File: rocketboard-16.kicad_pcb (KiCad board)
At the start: 2 copper layers, 86.2 x 99.9 mm, 110 parts, among them J1 SWD, K1 MX_RGB, K10 MX_RGB, K11 MX_RGB, K12 MX_RGB, K13 MX_RGB, K14 MX_RGB, K15 MX_RGB, K16 MX_RGB, K2 MX_RGB, K3 MX_RGB, K4 MX_RGB, K5 MX_RGB, K6 MX_RGB, K7 MX_RGB, K8 MX_RGB, K9 MX_RGB, P1 USB_C_Plug_USB2.0, SW1 SW_Push, SW2 Rotary 1, SW3 Rotary 2, U1 STM32F103C8T6, U2 AMS1117-3.3, U3 USBLC6-2SC6, U4 SSD1306_128x64, X1 8 MHz, Y1 32.768 kHz

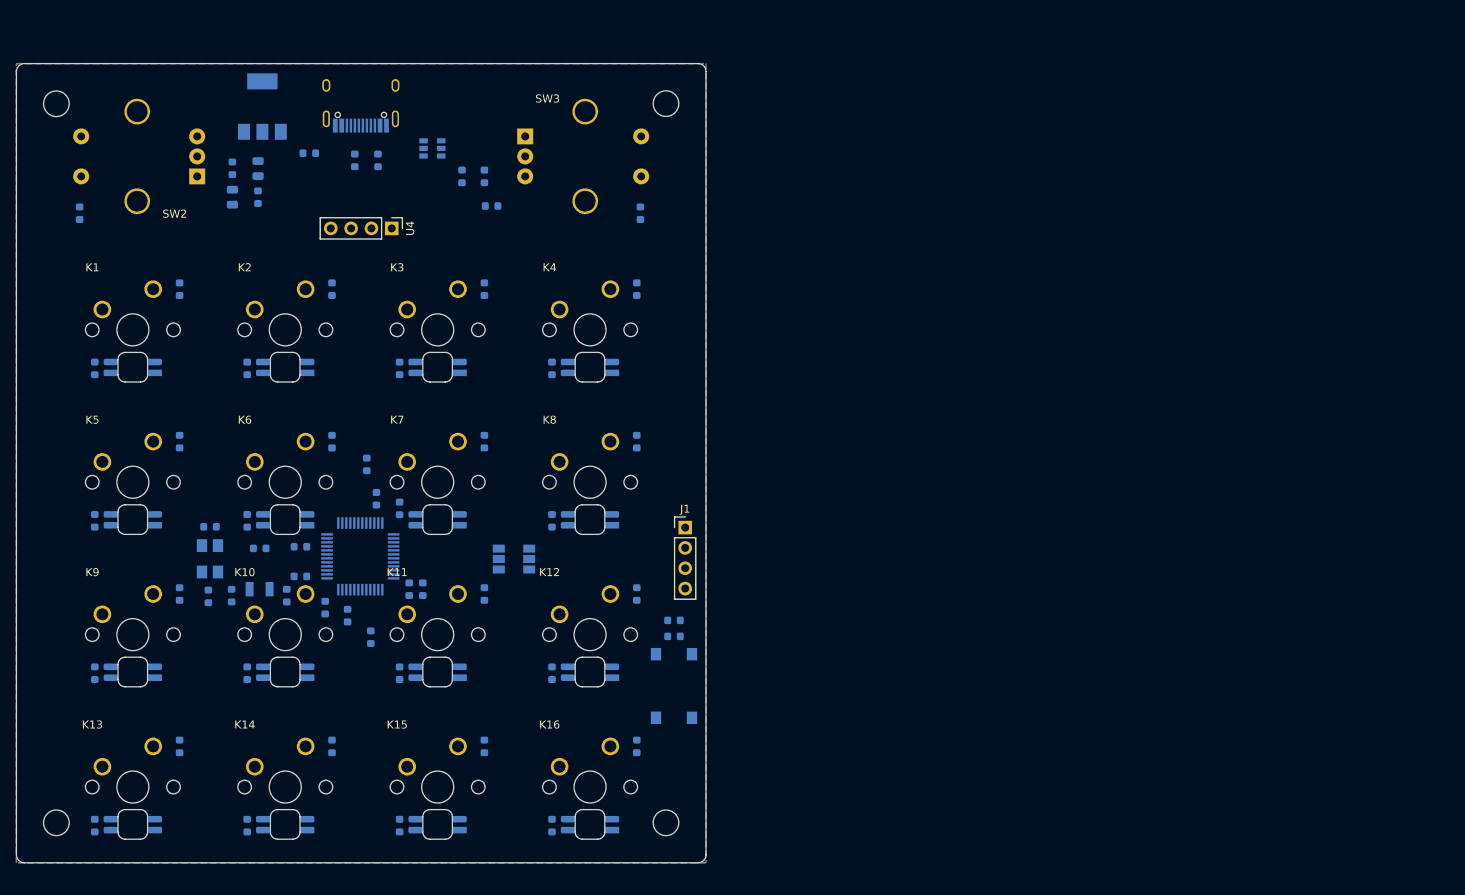
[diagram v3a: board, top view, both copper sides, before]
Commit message: Extended PCB height to accomodate the OLED display. Changed the board color to black for previews. Moved components up to take up new space from increasing height of board.
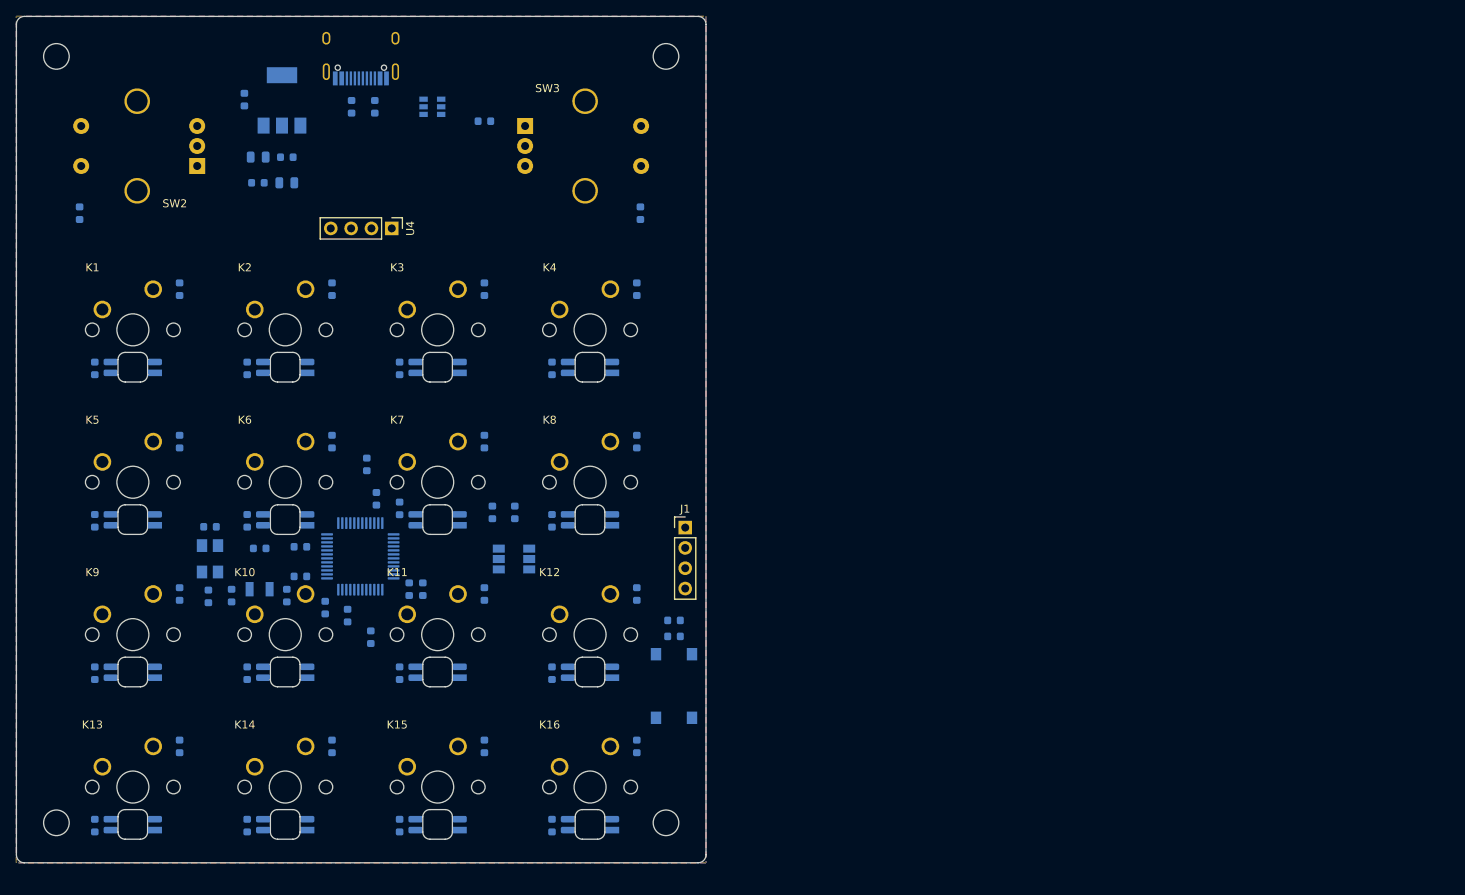
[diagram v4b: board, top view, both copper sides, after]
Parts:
- moved R1 42.5 mm to (142.3, 107.5), turned to 270 degrees
- moved R2 42.0 mm to (139.5, 107.5), turned to 270 degrees
- moved R6 10.6 mm to (138.5, 58.6)
- moved D17 10.5 mm to (108.5, 55.9), turned to 90 degrees
- moved C13 7.03 mm to (113.8, 66.3), turned to 180 degrees
- moved R5 6.71 mm to (124.8, 56.8)
- moved R4 6.71 mm to (121.9, 56.8)
- moved C14 6.16 mm to (113.8, 63.1), turned to 180 degrees
- moved H1 5.92 mm to (85.0, 50.5)
- moved H2 5.90 mm to (161.2, 50.5)
- moved P1 5.90 mm to (123.1, 50.1)
- moved U3 5.20 mm to (132.0, 56.8)
- moved C4 3.67 mm to (110.2, 66.3), turned to 0 degrees
- moved U2 2.57 mm to (113.2, 56.0)
- moved G*** 1.92 mm to (85.3, 124.8)
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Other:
- board size 86.2 x 99.9 mm -> 86.2 x 105.8 mm

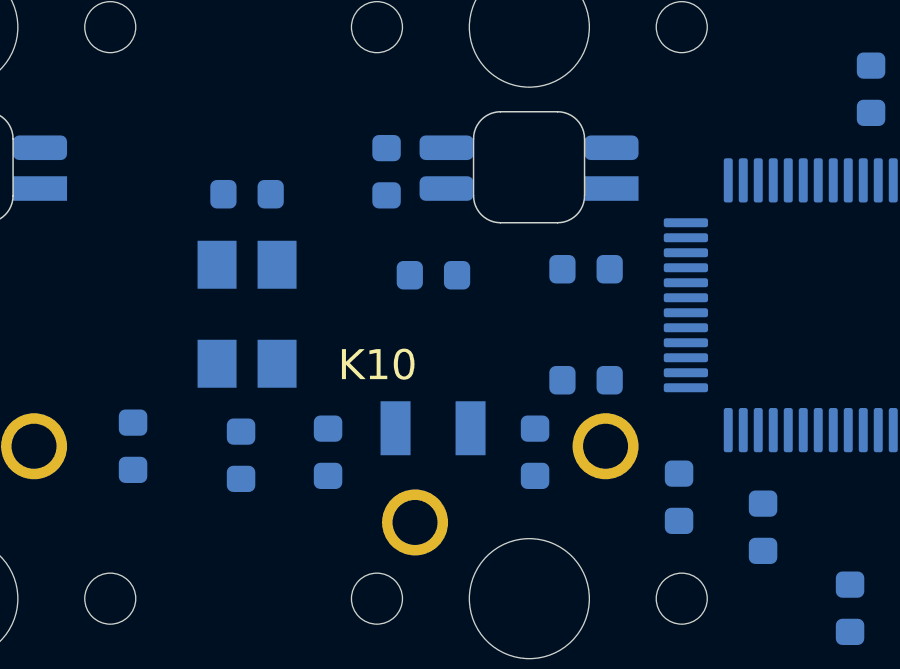
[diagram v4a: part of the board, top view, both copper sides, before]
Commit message: Routed the two crystals
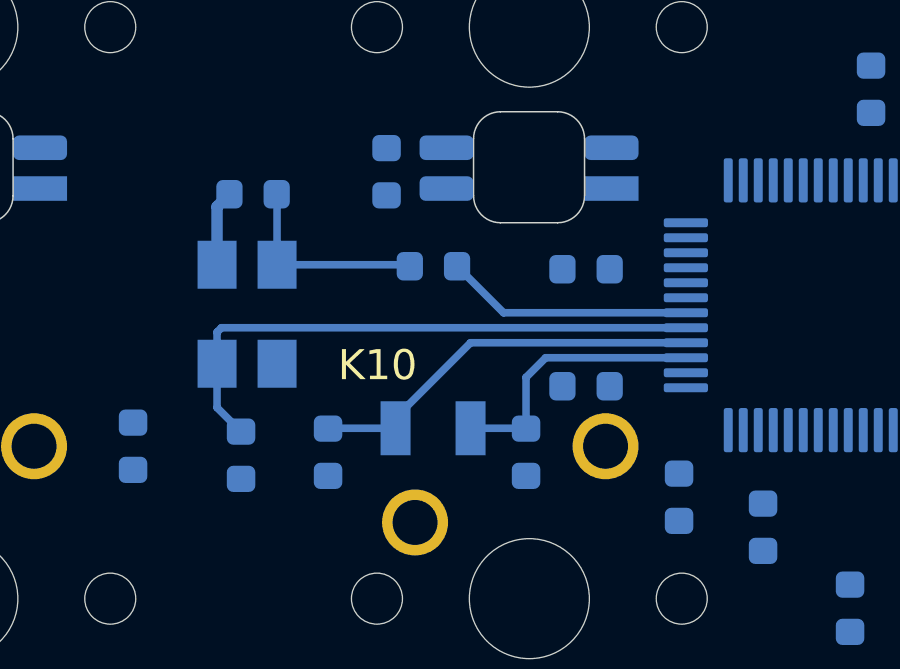
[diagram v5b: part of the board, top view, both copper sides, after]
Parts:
- moved C3 0.30 mm to (113.5, 117.9)
- moved R7 0.30 mm to (110.4, 111.7)
- moved C2 0.20 mm to (104.4, 109.3)
- moved C6 0.20 mm to (115.5, 115.7)
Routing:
- net OSC_IN: track 0.00 -> 19.3 mm
- net OSC32_OUT: track 0.00 -> 13.3 mm
- net OSC32_IN: track 0.00 -> 9.18 mm
- net OSC_OUT: track 0.00 -> 8.27 mm
- net Net-(C2-Pad1): track 0.00 -> 6.80 mm
- net GND: track 0.00 -> 2.52 mm
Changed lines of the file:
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@@
     (thickness 1.6)
     (drawings 13)
-    (tracks 0)
+    (tracks 24)
     (zones 0)
     (modules 110)
@@
   )
   (module Capacitor_SMD:C_0603_1608Metric (layer B.Cu)
-    (at 115.5 115.5)
+    (at 115.5 115.7)
     (descr "Capacitor SMD 0603 (1608 Metric), square (rectangular) end terminal, IPC_7351 nominal, (Body size source: http://www.tortai-tech.com/upload/download/2011102023233369053.pdf), generated with kicad-footprint-generator")
     (tags capacitor)
@@
   )
   (module Capacitor_SMD:C_0603_1608Metric (layer B.Cu)
-    (at 113.8 117.9 270)
+    (at 113.5 117.9 270)
     (descr "Capacitor SMD 0603 (1608 Metric), square (rectangular) end terminal, IPC_7351 nominal, (Body size source: http://www.tortai-tech.com/upload/download/2011102023233369053.pdf), generated with kicad-footprint-generator")
     (tags capacitor)
@@
       (effects (font (size 1 1) (thickness 0.15)) (justify mirror))
     )
-    (fp_line (start 1.48 -0.73) (end -1.48 -0.73) (layer B.CrtYd) (width 0.05))
-    (fp_line (start 1.48 0.73) (end 1.48 -0.73) (layer B.CrtYd) (width 0.05))
-    (fp_line (start -1.48 0.73) (end 1.48 0.73) (layer B.CrtYd) (width 0.05))
-    (fp_line (start -1.48 -0.73) (end -1.48 0.73) (layer B.CrtYd) (width 0.05))
-    (fp_line (start -0.162779 -0.51) (end 0.162779 -0.51) (layer B.SilkS) (width 0.12))
-    (fp_line (start -0.162779 0.51) (end 0.162779 0.51) (layer B.SilkS) (width 0.12))
-    (fp_line (start 0.8 -0.4) (end -0.8 -0.4) (layer B.Fab) (width 0.1))
-    (fp_line (start 0.8 0.4) (end 0.8 -0.4) (layer B.Fab) (width 0.1))
-    (fp_line (start -0.8 0.4) (end 0.8 0.4) (layer B.Fab) (width 0.1))
-    (fp_line (start -0.8 -0.4) (end -0.8 0.4) (layer B.Fab) (width 0.1))
     (fp_text user %R (at 0 0 270) (layer B.Fab)
       (effects (font (size 0.4 0.4) (thickness 0.06)) (justify mirror))
     )
-    (pad 2 smd roundrect (at 0.7875 0 270) (size 0.875 0.95) (layers B.Cu B.Paste B.Mask) (roundrect_rratio 0.25)
-      (net 24 GND))
+    (fp_line (start -0.8 -0.4) (end -0.8 0.4) (layer B.Fab) (width 0.1))
+    (fp_line (start -0.8 0.4) (end 0.8 0.4) (layer B.Fab) (width 0.1))
+    (fp_line (start 0.8 0.4) (end 0.8 -0.4) (layer B.Fab) (width 0.1))
+    (fp_line (start 0.8 -0.4) (end -0.8 -0.4) (layer B.Fab) (width 0.1))
+    (fp_line (start -0.162779 0.51) (end 0.162779 0.51) (layer B.SilkS) (width 0.12))
+    (fp_line (start -0.162779 -0.51) (end 0.162779 -0.51) (layer B.SilkS) (width 0.12))
+    (fp_line (start -1.48 -0.73) (end -1.48 0.73) (layer B.CrtYd) (width 0.05))
+    (fp_line (start -1.48 0.73) (end 1.48 0.73) (layer B.CrtYd) (width 0.05))
+    (fp_line (start 1.48 0.73) (end 1.48 -0.73) (layer B.CrtYd) (width 0.05))
+    (fp_line (start 1.48 -0.73) (end -1.48 -0.73) (layer B.CrtYd) (width 0.05))
     (pad 1 smd roundrect (at -0.7875 0 270) (size 0.875 0.95) (layers B.Cu B.Paste B.Mask) (roundrect_rratio 0.25)
       (net 27 OSC32_IN))
+    (pad 2 smd roundrect (at 0.7875 0 270) (size 0.875 0.95) (layers B.Cu B.Paste B.Mask) (roundrect_rratio 0.25)
+      (net 24 GND))
     (model ${KISYS3DMOD}/Capacitor_SMD.3dshapes/C_0603_1608Metric.wrl
       (at (xyz 0 0 0))
@@
   )
   (module Resistor_SMD:R_0603_1608Metric (layer B.Cu)
-    (at 110.4125 112)
+    (at 110.4125 111.7)
     (descr "Resistor SMD 0603 (1608 Metric), square (rectangular) end terminal, IPC_7351 nominal, (Body size source: http://www.tortai-tech.com/upload/download/2011102023233369053.pdf), generated with kicad-footprint-generator")
     (tags resistor)
@@
   )
   (module Capacitor_SMD:C_0603_1608Metric (layer B.Cu)
-    (at 104.2 109.3 180)
+    (at 104.4 109.3 180)
     (descr "Capacitor SMD 0603 (1608 Metric), square (rectangular) end terminal, IPC_7351 nominal, (Body size source: http://www.tortai-tech.com/upload/download/2011102023233369053.pdf), generated with kicad-footprint-generator")
     (tags capacitor)
@@
     (arrow2b (pts (xy 80 41.4) (xy 81.126504 40.813579)))
   )
+  (segment (start 103.2 109.7125) (end 103.6125 109.3) (width 0.381) (layer B.Cu) (net 24))
+  (segment (start 103.2 111.65) (end 103.2 109.7125) (width 0.381) (layer B.Cu) (net 24))
+  (segment (start 103.2 116.4125) (end 104 117.2125) (width 0.254) (layer B.Cu) (net 25))
+  (segment (start 103.2 114.95) (end 103.2 116.4125) (width 0.254) (layer B.Cu) (net 25))
+  (segment (start 103.346 113.75) (end 118.8275 113.75) (width 0.254) (layer B.Cu) (net 25))
+  (segment (start 103.2 113.896) (end 103.346 113.75) (width 0.254) (layer B.Cu) (net 25))
+  (segment (start 103.2 114.95) (end 103.2 113.896) (width 0.254) (layer B.Cu) (net 25))
+  (segment (start 105.2 109.3125) (end 105.1875 109.3) (width 0.254) (layer B.Cu) (net 26))
+  (segment (start 105.2 111.65) (end 105.2 109.3125) (width 0.254) (layer B.Cu) (net 26))
+  (segment (start 109.575 111.65) (end 109.625 111.7) (width 0.254) (layer B.Cu) (net 26))
+  (segment (start 105.2 111.65) (end 109.575 111.65) (width 0.254) (layer B.Cu) (net 26))
+  (segment (start 113.7875 117.1) (end 113.8 117.1125) (width 0.254) (layer B.Cu) (net 27))
+  (segment (start 113.4875 117.1) (end 113.5 117.1125) (width 0.254) (layer B.Cu) (net 27))
+  (segment (start 111.65 117.1) (end 113.4875 117.1) (width 0.254) (layer B.Cu) (net 27))
+  (segment (start 113.5 117.1125) (end 113.5 115.40401) (width 0.254) (layer B.Cu) (net 27))
+  (segment (start 114.15401 114.75) (end 118.8275 114.75) (width 0.254) (layer B.Cu) (net 27))
+  (segment (start 113.5 115.40401) (end 114.15401 114.75) (width 0.254) (layer B.Cu) (net 27))
+  (segment (start 106.9125 117.1) (end 106.9 117.1125) (width 0.254) (layer B.Cu) (net 29))
+  (segment (start 109.15 117.1) (end 106.9125 117.1) (width 0.254) (layer B.Cu) (net 29))
+  (segment (start 109.15 117.1) (end 109.15 116.75) (width 0.254) (layer B.Cu) (net 29))
+  (segment (start 111.65 114.25) (end 118.8275 114.25) (width 0.254) (layer B.Cu) (net 29))
+  (segment (start 109.15 116.75) (end 111.65 114.25) (width 0.254) (layer B.Cu) (net 29))
+  (segment (start 112.75 113.25) (end 118.8275 113.25) (width 0.254) (layer B.Cu) (net 54))
+  (segment (start 111.2 111.7) (end 112.75 113.25) (width 0.254) (layer B.Cu) (net 54))
   (zone (net 24) (net_name GND) (layer F.Cu) (hatch edge 0.508)
     (connect_pads (clearance 0.508))

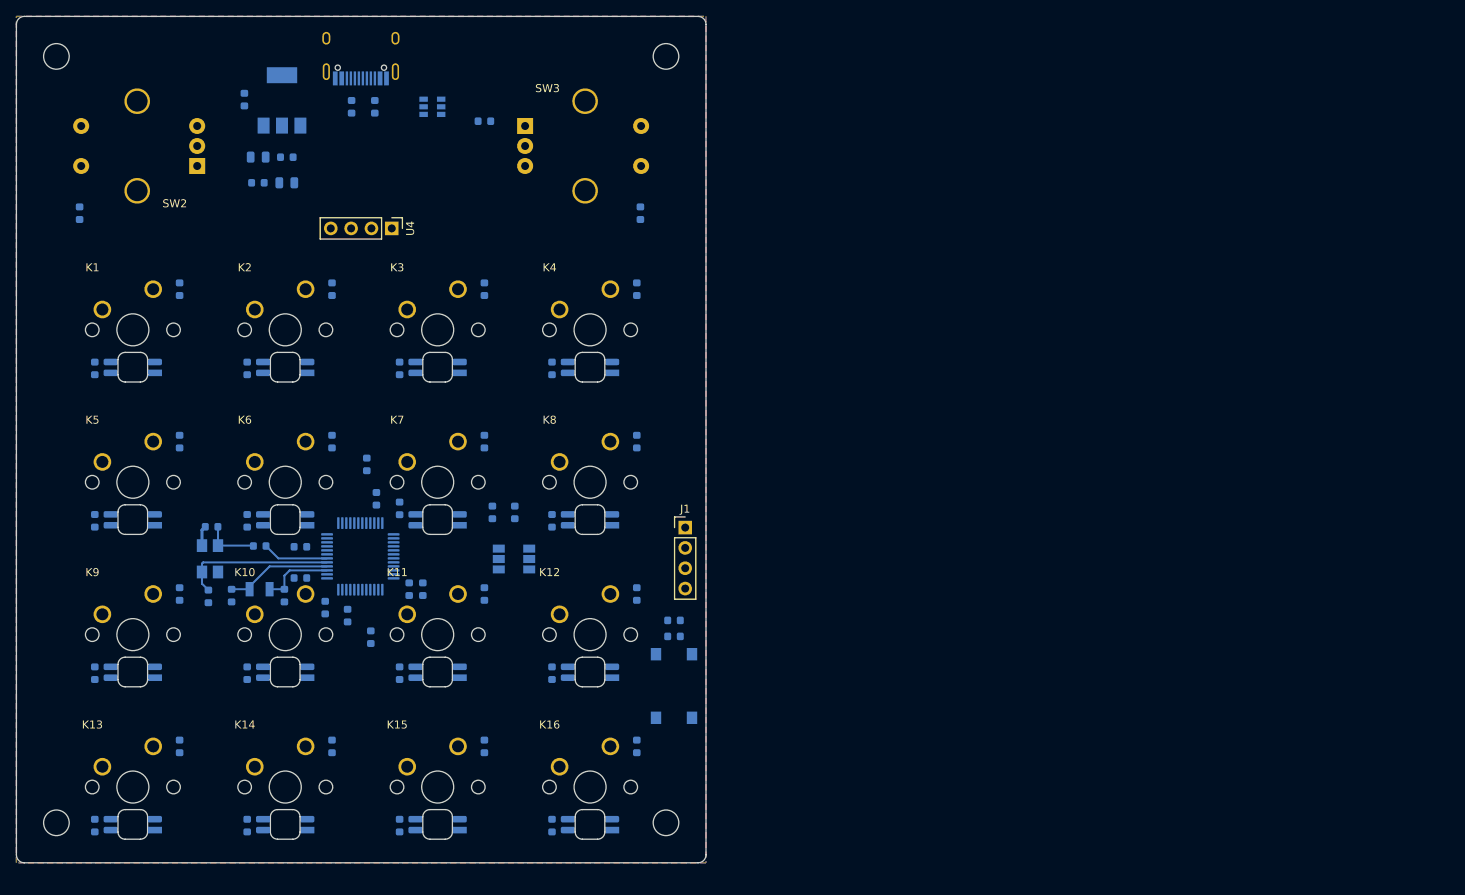
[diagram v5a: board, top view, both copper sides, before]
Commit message: Routed most of the wires, many still needed though. Changed a couple of pins around on the schematic due to simpler routing paths.
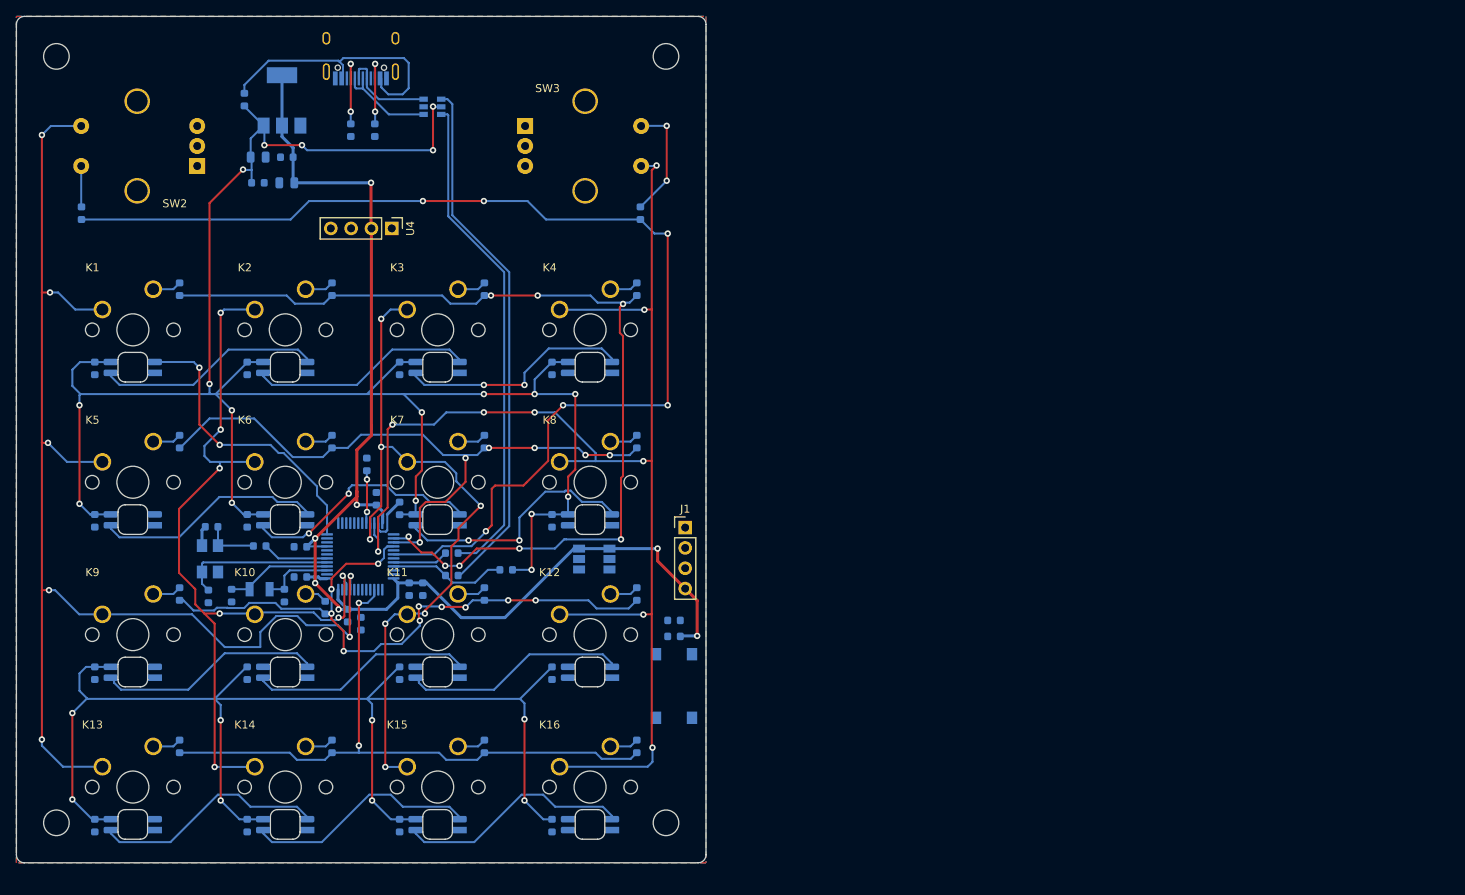
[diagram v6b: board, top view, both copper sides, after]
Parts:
- moved R6 56.1 mm to (141.2, 114.7)
- moved JP2 10.0 mm to (154.1, 113.3)
- moved JP1 10.0 mm to (150.3, 113.3)
- moved R2 9.38 mm to (134.4, 115.4), turned to 0 degrees
- moved R1 9.38 mm to (134.4, 112.6), turned to 0 degrees
- moved R4 2.92 mm to (121.8, 59.7)
- moved R5 2.92 mm to (124.8, 59.7)
- moved R8 2.09 mm to (123.1, 121.4)
- moved D18 0.24 mm to (88.1, 70.1)
- moved C6 0.13 mm to (115.5, 115.6), turned to 180 degrees
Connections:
- U1 pad 13: Row4 -> Net-(U1-Pad13)
- U1 pad 25: ROW0 -> Net-(U1-Pad25)
- U1 pad 30: Net-(U1-Pad30) -> ROW0
- U1 pad 39: Net-(U1-Pad39) -> Row4
- U4 pad 1: Net-(U4-Pad1) -> GND
- U4 pad 2: Net-(U4-Pad2) -> VCC
- U4 pad 3: Net-(U4-Pad3) -> SCL
- U4 pad 4: Net-(U4-Pad4) -> SDA
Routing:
- net +5V: track 0.00 -> 404.7 mm, vias 0 -> 26
- net COL3: track 0.00 -> 172.9 mm, vias 0 -> 9
- net COL0: track 0.00 -> 162.0 mm, vias 0 -> 7
- net VCC: track 0.00 -> 161.9 mm, vias 0 -> 7
- net ROW0: track 0.00 -> 145.1 mm, vias 0 -> 6
- net ROW1: track 0.00 -> 121.2 mm, vias 0 -> 8
- net COL1: track 0.00 -> 102.2 mm, vias 0 -> 7
- net COL2: track 0.00 -> 92.5 mm, vias 0 -> 7
- net ROW3: track 0.00 -> 82.1 mm, vias 0 -> 10
- net ROW2: track 0.00 -> 82.0 mm, vias 0 -> 6
- net Row4: track 0.00 -> 81.1 mm, vias 0 -> 2
- net Net-(R2-Pad2): track 0.00 -> 66.4 mm
- net Net-(R1-Pad2): track 0.00 -> 62.3 mm
- net LED_SIG: track 0.00 -> 37.4 mm, vias 0 -> 2
- net Net-(D17-Pad2): track 0.00 -> 34.0 mm
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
